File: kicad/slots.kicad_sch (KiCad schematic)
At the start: 98 parts, among them J19 2.54-2*3P, J20 2.54-2*3P, J3 WingTAT 2044-2X32G00SA, J5 WingTAT 2044-2X32G00SA, J53 XFCN PM254V-11-07-H85, J54 XFCN PM254V-11-07-H85, J55 XFCN PM254V-11-07-H85, J56 XFCN PM254V-11-07-H85, J57 XFCN PM254V-11-07-H85, J58 XFCN PM254V-11-07-H85, J62 XFCN PM254V-11-07-H85, J63 XFCN PM254V-11-07-H85, J64 XFCN PM254V-11-07-H85, J65 XFCN PM254V-11-07-H85, J7 PM254-2-08-Z-8.5, J8 PM254-2-08-Z-8.5, U10 SN74LXC8T245PWR, U9 SN74LXC8T245PWR

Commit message: Explain the remaining four sheets: power, memory, board controller, slots
Every part and group on the board now has its plain-words purpose, and the
gate enforces it on all six sheets. Net notes can cover a family of nets
by prefix, so regulator feedback, enables and the PSRAM series resistors
read correctly; passives credit their group's IC or connector rather than
a key post; monitor nets are no longer mistaken for supplies; parts that
are not fitted say so. PCB synced with no footprint moved.
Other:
- note added: "Jumper that picks the signal voltage of slots A-D: one shunt on J19 selects 3.3, 2.5 or 1.8 V. It powers FPGA bank 15 and the PIN V pin of those four slots. One position only; change it with the board unpowered."
- note added: "Jumper that picks the signal voltage of slots E-H (J20): 3.3, 2.5 or 1.8 V for FPGA bank 34 and those slots' PIN V pin."
- note added: "Lets the FPGA (3.3 V) talk to 5 V extensions on slot L. U9 shifts eight lines between 3.3 V and 5 V, all in one direction at a time (BUS5V0_DIR). It stays off until the FPGA pulls BUS5V0_OE_N low; the pull-up keeps the bus off while the FPGA is still loading."
- note added: "One long 2x32 socket on the left edge carrying the signals of slots E, F, G and H: twelve FPGA pins each (bank 34), voltage set by J20."
- note added: "One long 2x32 socket on the right edge carrying the signals of slots A, B, C and D: twelve FPGA pins each (bank 15), with grounds between groups. Their voltage is whatever J19 selects."
- note added: "Power for whatever is plugged into slot A. The 1x7 power socket carries PIN V (the J19 voltage), 3.3 V, 5 V and AUX, each beside a ground, and each through its own resettable fuse, so a short on one extension trips only that slot's fuse and the rest of the board keeps running. The long grounded pin in front of the socket is the key that stops an extension going in the wrong way, and a ground prob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"
- note added: "Power for whatever is plugged into slot B. The 1x7 power socket carries PIN V (the J19 voltage), 3.3 V, 5 V and AUX, each beside a ground, and each through its own resettable fuse, so a short on one extension trips only that slot's fuse and the rest of the board keeps running. The long grounded pin in front of the socket is the key that stops an extension going in the wrong way, and a ground prob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"
- note added: "Power for whatever is plugged into slot C. The 1x7 power socket carries PIN V (the J19 voltage), 3.3 V, 5 V and AUX, each beside a ground, and each through its own resettable fuse, so a short on one extension trips only that slot's fuse and the rest of the board keeps running. The long grounded pin in front of the socket is the key that stops an extension going in the wrong way, and a ground prob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"
- note added: "Power for whatever is plugged into slot D. The 1x7 power socket carries PIN V (the J19 voltage), 3.3 V, 5 V and AUX, each beside a ground, and each through its own resettable fuse, so a short on one extension trips only that slot's fuse and the rest of the board keeps running. The long grounded pin in front of the socket is the key that stops an extension going in the wrong way, and a ground prob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"
- note added: "Power for whatever is plugged into slot E. The 1x7 power socket carries PIN V (the J20 voltage), 3.3 V, 5 V and AUX, each beside a ground, and each through its own resettable fuse, so a short on one extension trips only that slot's fuse and the rest of the board keeps running. The long grounded pin in front of the socket is the key that stops an extension going in the wrong way, and a ground prob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"
- note added: "Power for whatever is plugged into slot F. The 1x7 power socket carries PIN V (the J20 voltage), 3.3 V, 5 V and AUX, each beside a ground, and each through its own resettable fuse, so a short on one extension trips only that slot's fuse and the rest of the board keeps running. The long grounded pin in front of the socket is the key that stops an extension going in the wrong way, and a ground prob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"
- note added: "Power for whatever is plugged into slot G. The 1x7 power socket carries PIN V (the J20 voltage), 3.3 V, 5 V and AUX, each beside a ground, and each through its own resettable fuse, so a short on one extension trips only that slot's fuse and the rest of the board keeps running. The long grounded pin in front of the socket is the key that stops an extension going in the wrong way, and a ground prob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"
- note added: "Power for whatever is plugged into slot H. The 1x7 power socket carries PIN V (the J20 voltage), 3.3 V, 5 V and AUX, each beside a ground, and each through its own resettable fuse, so a short on one extension trips only that slot's fuse and the rest of the board keeps running. The long grounded pin in front of the socket is the key that stops an extension going in the wrong way, and a ground prob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"
- note added: "Power for whatever is plugged into slot L. The 1x7 power socket carries PIN V (3.3 V), 3.3 V, 5 V and AUX, each beside a ground, and each through its own resettable fuse, so a short on one extension trips only that slot's fuse and the rest of the board keeps running. The long grounded pin in front of the socket is the key that stops an extension going in the wrong way, and a ground probe point."
- note added: "Power for whatever is plugged into slot M. The 1x7 power socket carries PIN V (3.3 V), 3.3 V, 5 V and AUX, each beside a ground, and each through its own resettable fuse, so a short on one extension trips only that slot's fuse and the rest of the board keeps running. The long grounded pin in front of the socket is the key that stops an extension going in the wrong way, and a ground probe point."
- note added: "Same as 5V BUS 0, for slot M: U10 shifts eight lines between the FPGA's 3.3 V and 5 V, direction BUS5V1_DIR, off until BUS5V1_OE_N goes low."
- note added: "The signal socket of slot L (5V BUS 0): eight 5 V data lines from U9, with four grounds between them."
- note added: "The signal socket of slot M (5V BUS 1): eight 5 V data lines from U10, with four grounds between them."
- moved on the sheet: C139, C140, C141, C142, C143, C144, C145, C146, C147, C148, C149, C150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

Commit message: Step 1: the +1V8_IO rail
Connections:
- net +1V8 renamed +1V8_IO

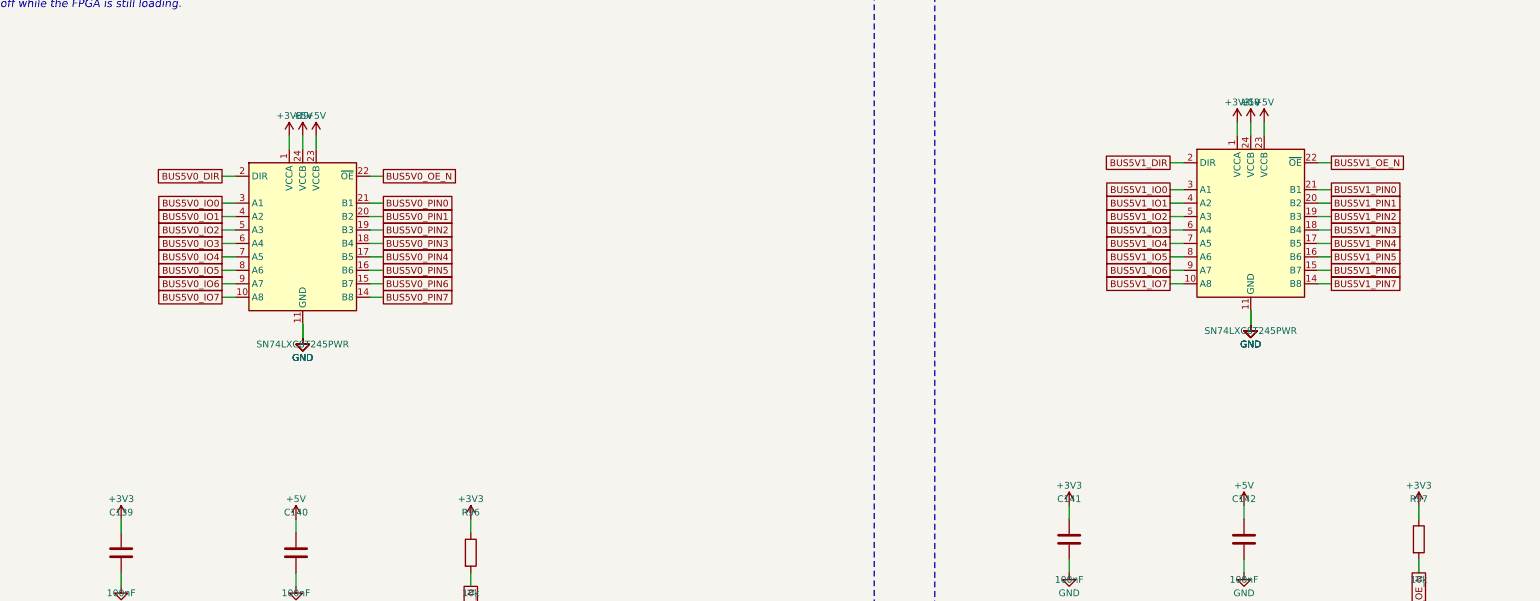
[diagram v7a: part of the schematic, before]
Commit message: Step 2: bank 13 to 1.8V and the PSRAM move
SN74LXC8T245 datasheet SCES916A (rev. March 2023), section 6.3
Recommended Operating Conditions, page 5: VCCA 1.08 V to 5.5 V, so the
A side runs from +1V8_IO. Table 5-1 (page 3) states the same range on
the VCCA pin. Copy in ref/datasheets/sn74lxc8t245.pdf.

APS6404L-SQN-SN: datasheet rev 4.0, Table 9 page 26 (VDD 1.62 to 1.98 V,
ICC 7 mA), section 4.1 page 5 (SOP-8L(150): D 4.90, E1 3.90, E 6.00 BSC,
e 1.27 BSC), which the fitted SOIC-8_L4.9-W3.9-P1.27-LS6.0-BL matches.
Copy in ref/datasheets/aps6404l-sqn.pdf. The symbol for C5360304 is
imported into easyeda/EasyEDA.kicad_sym pointing at that footprint, and
load_pcb.py now refreshes the LCSC field on every sync.
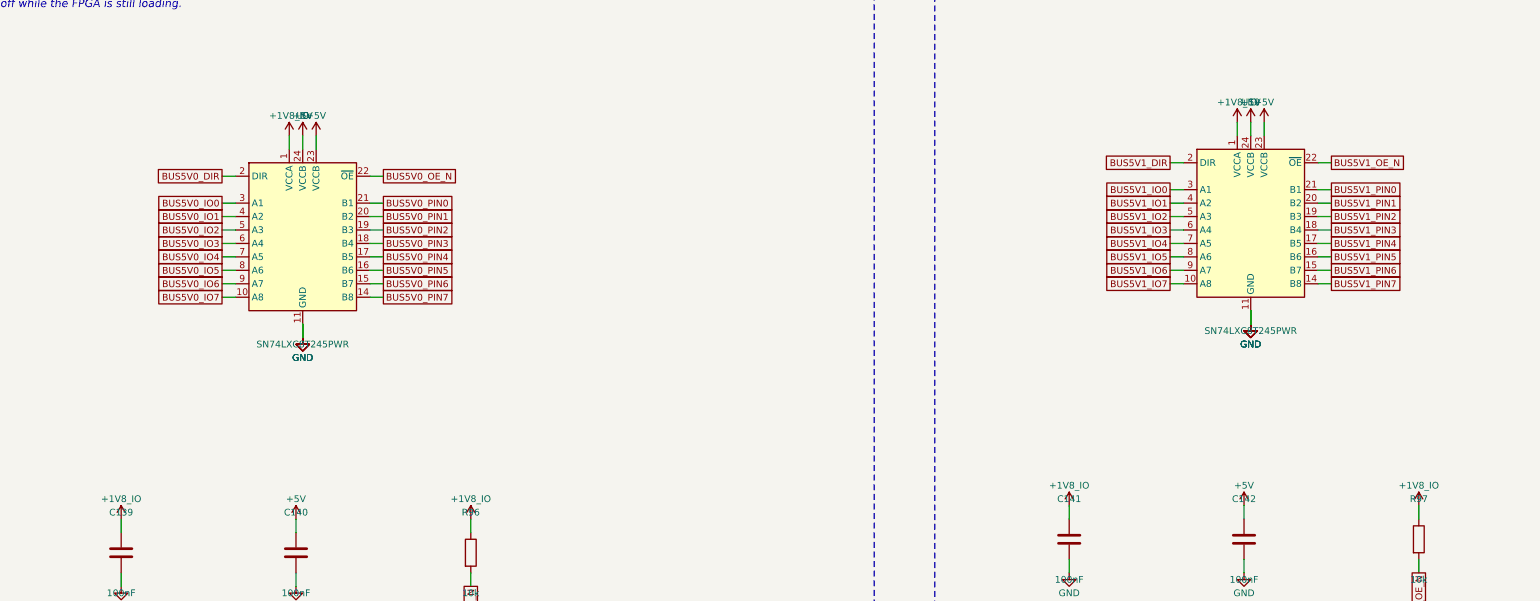
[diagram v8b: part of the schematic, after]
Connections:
- net +1V8_IO: now also C139.1, C141.1, R96.1, R97.1, U10.1 (VCCA), U9.1 (VCCA)
- net +3V3: no longer C139.1, C141.1, R96.1, R97.1, U10.1 (VCCA), U9.1 (VCCA)
